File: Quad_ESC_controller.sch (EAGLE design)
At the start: 24 parts, among them Y1 ECS-80-S-4X

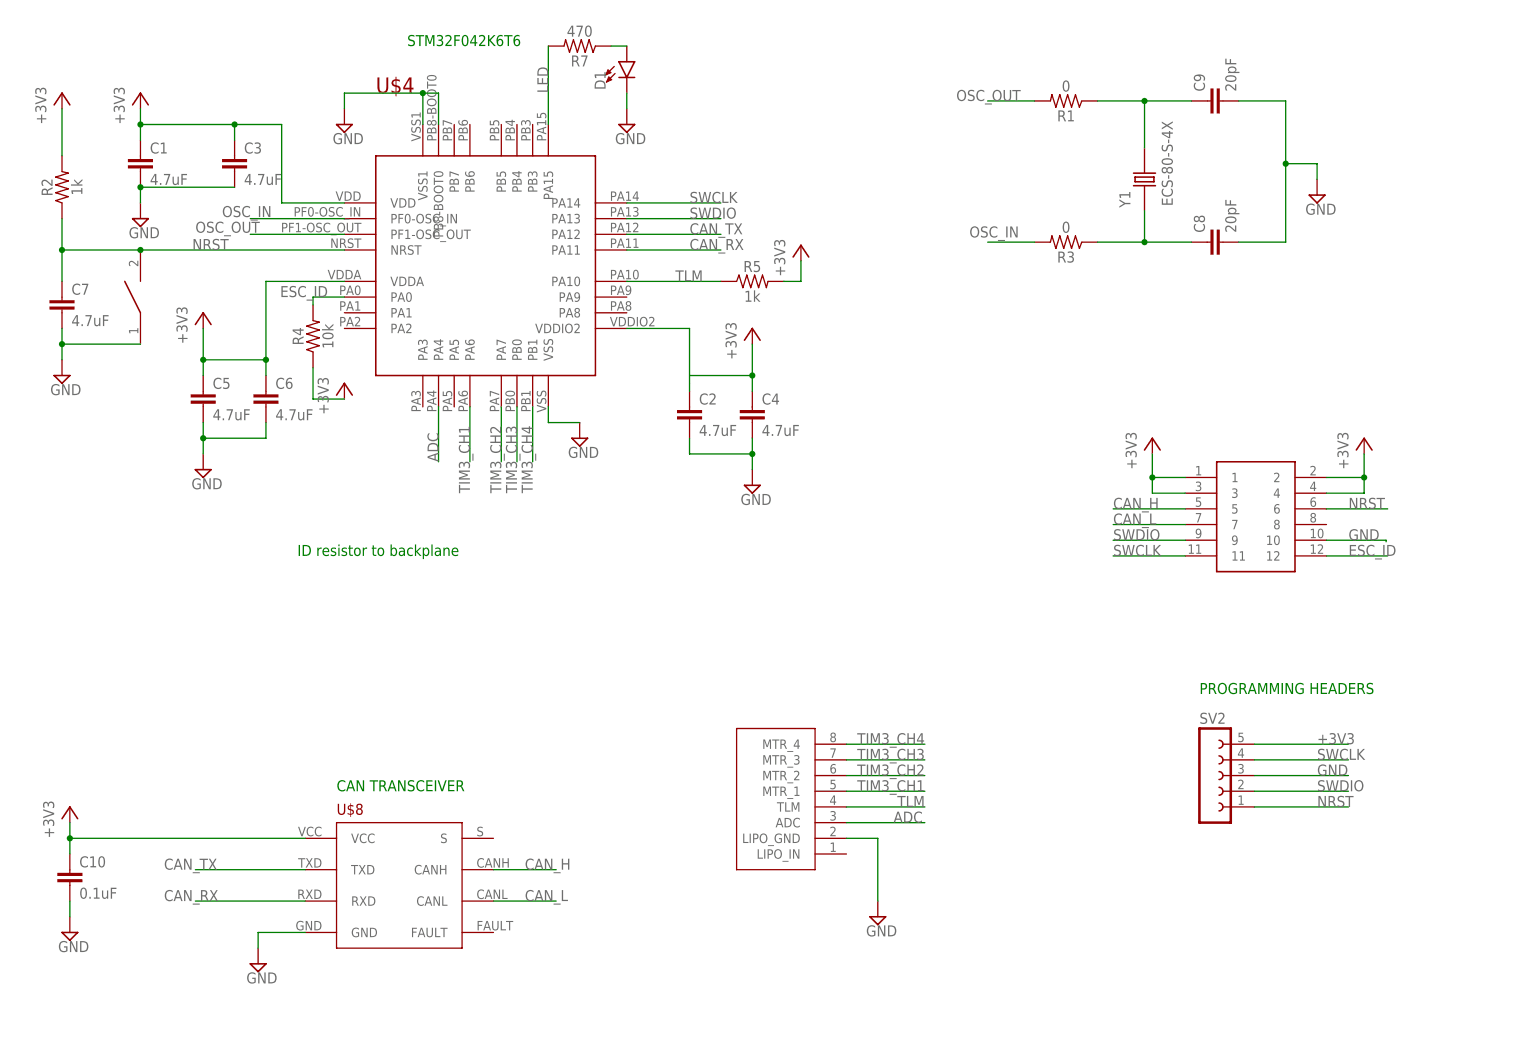
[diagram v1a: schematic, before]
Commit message: Add op amp for telemetry logic level fixing
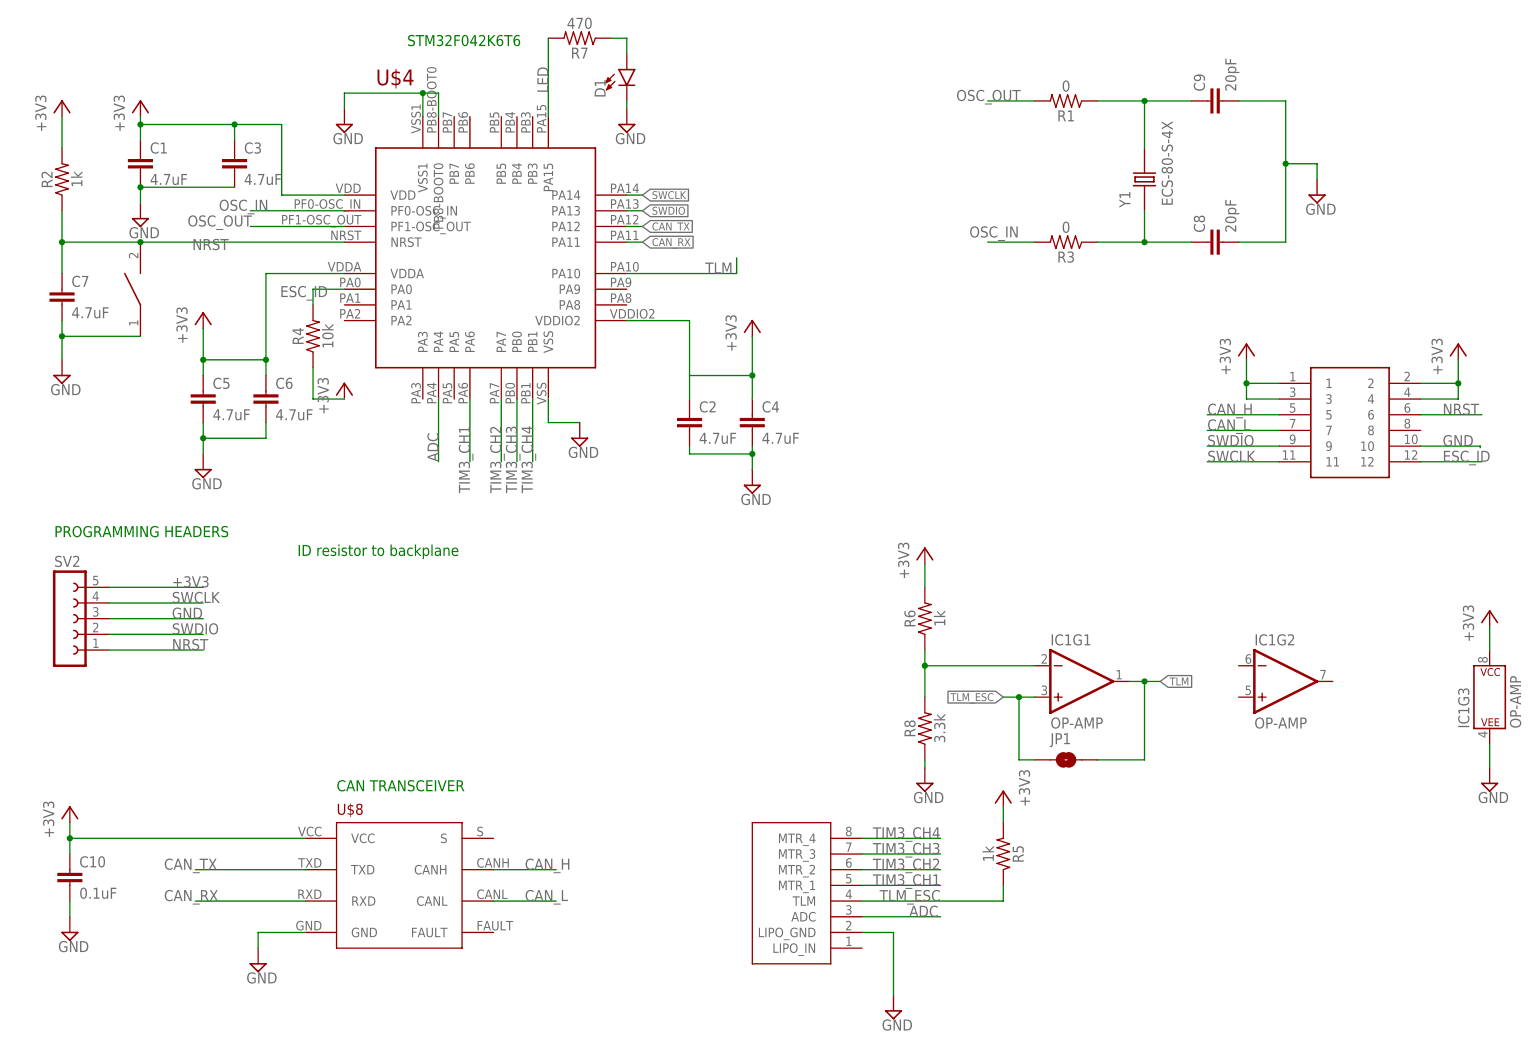
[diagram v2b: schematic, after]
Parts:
- added IC1: OP-AMP, SparkFun-IC-Amplifiers:OPAMP-DUALU
- added JP1: JUMPER-SMT_2_NO_SILK, SparkFun-Jumpers:JUMPER-SMT_2_NO_SILK
- added R6: 1k, SparkFun-Resistors:RESISTOR0603
- added R8: 3.3k, SparkFun-Resistors:RESISTOR0603
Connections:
- new net N$6: IC1G1.-IN, R6.1, R8.2
- new net TLM_ESC: IC1G1.+IN, JP1.1, R5.1, U$2.TLM
- net +3V3: now also IC1G3.P$V+, R6.2
- net GND: now also IC1G3.P$V-, R8.1
- net TLM: now also IC1G1.OUT, JP1.2; no longer R5.1, U$2.TLM
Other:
- moved on the sheet: C2, C4, C7, D1, R2, R5, R7, SV2, U$4

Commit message: New SWD programming connector
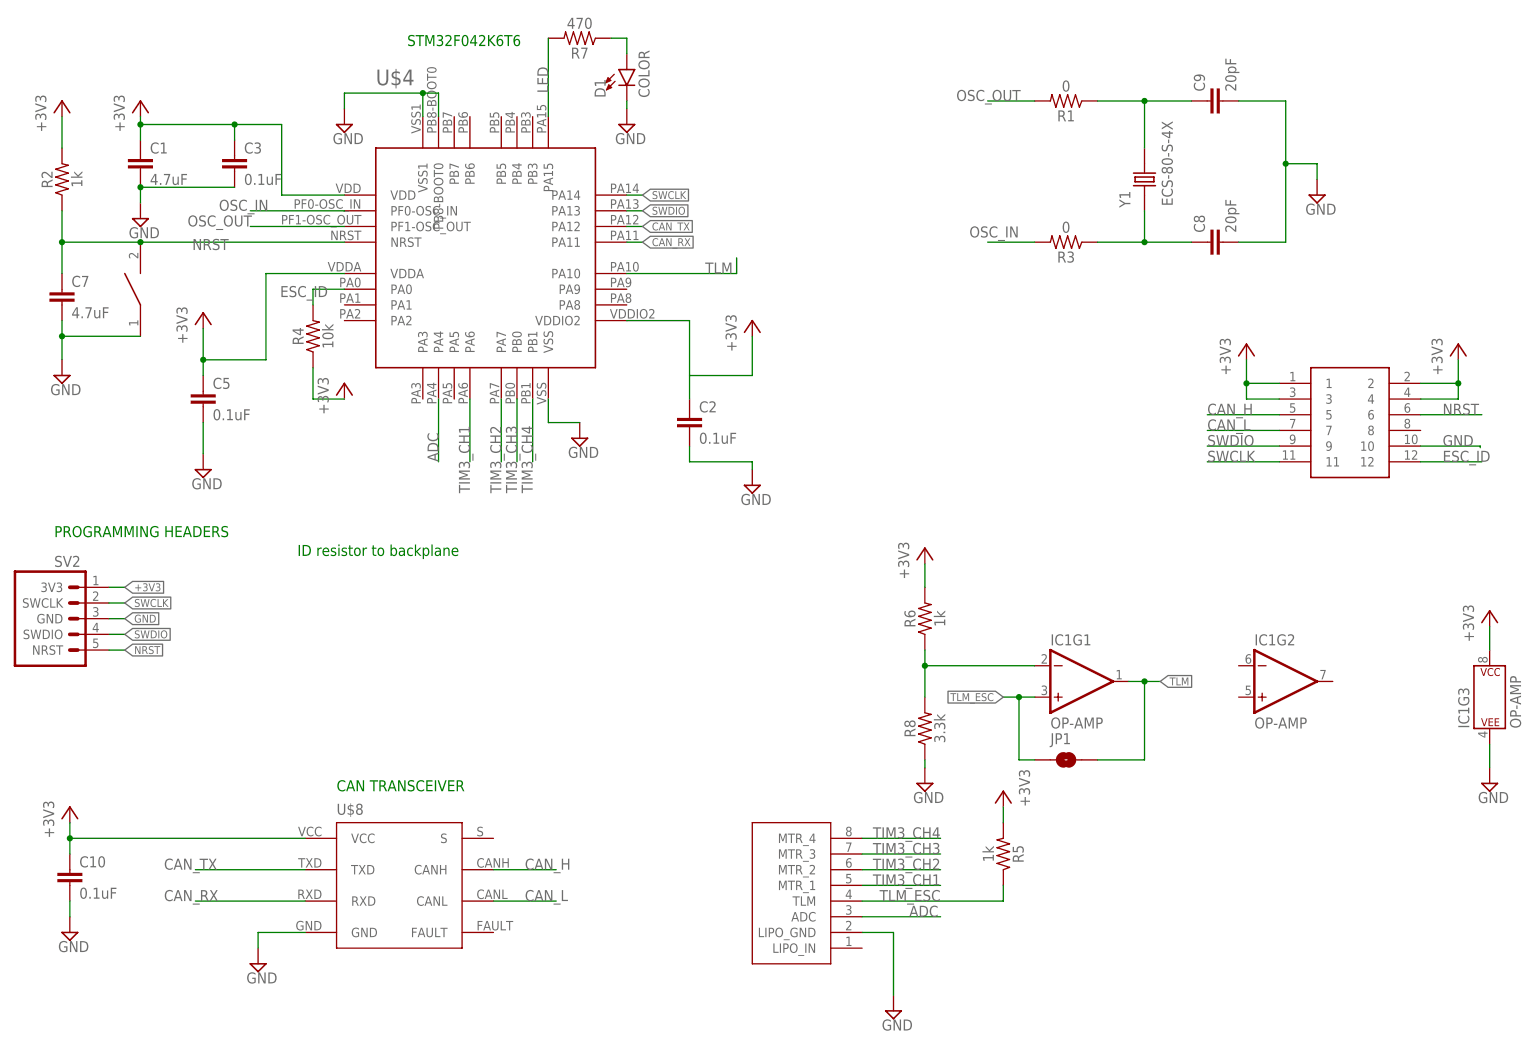
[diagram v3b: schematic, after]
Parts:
- removed C4, C6: 4.7uF, SparkFun-Capacitors:4.7UF0603
- C2, C3, C5: value 4.7uF -> 0.1uF
- D1: value (none) -> COLOR; device SparkFun-LED:LED0603 -> LED, 0805:LED-0805
- SV2: value (none) -> 3V3 -SWCLK-GND-SWDIO- NRST; device con-lsta:FE05-1 -> CONN, Serial Wire Programming Headers:SWD_CONN
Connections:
- net +3V3: now also SV2.3V3; no longer C4.1, C6.1, SV2.5
- net GND: now also SV2.GND; no longer C4.2, C6.2, SV2.3
- net NRST: now also SV2.NRST; no longer SV2.1
- net SWCLK: now also SV2.SWCLK; no longer SV2.4
- net SWDIO: now also SV2.SWDIO; no longer SV2.2

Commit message: Use aluminum caps for the adapter board
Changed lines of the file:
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@@
 <text x="16.51" y="91.948" size="1.778" layer="91">PROGRAMMING HEADERS</text>
 <text x="62.23" y="50.8" size="1.778" layer="91">CAN TRANSCEIVER</text>
-<text x="55.88" y="88.9" size="1.778" layer="91">ID resistor to backplane</text>
+<text x="50.8" y="109.22" size="1.778" layer="91">ID resistor to backplane</text>
 </plain>
 <instances>
@@
 <segment>
 <pinref part="U$4" gate="G$1" pin="PA10"/>
-<wire x1="109.22" y1="134.62" x2="127" y2="134.62" width="0.1524" layer="91"/>
+<wire x1="109.22" y1="134.62" x2="121.92" y2="134.62" width="0.1524" layer="91"/>
 <label x="121.92" y="134.62" size="1.778" layer="95"/>
-<wire x1="127" y1="134.62" x2="127" y2="137.16" width="0.1524" layer="91"/>
-</segment>
-<segment>
+</segment>
+<segment>
